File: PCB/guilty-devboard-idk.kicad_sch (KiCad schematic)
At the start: 66 parts, among them J1 USB_C_Receptacle_USB2.0_16P, Q1 SP2038CNQ, Q2 Q_PMOS, U1 nRF54LM20A-PAXX, U2 SGM40567-4.2XG/TR, U3 Xiao nRF52840 Connectors, U4 MIC2876-5.0YMT-TR, U5 FH9261-G3JH, U6 BD83070GWL-E2, Y1 32MHz, Y2 32.768kHz

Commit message: fully routed
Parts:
- removed C10: 4.7uF, Capacitor_SMD:C_0201_0603Metric, symbol KiCad:C_Small
- removed C20: 22uF, Capacitor_SMD:C_0201_0603Metric, symbol Device:C
- removed C22: 1uF, Capacitor_SMD:C_0201_0603Metric, symbol Device:C_Small
- removed D2, D3: D, Diode_SMD:D_SOD-882, symbol Device:D
- removed D4, D5: D, Diode_SMD:D_SOD-323, symbol Device:D
- removed JP2: Jumper_2_Bridged, Resistor_SMD:R_0201_0603Metric, symbol KiCad:Jumper_2_Bridged
- removed L2: 2.2uH, Inductor_SMD:L_0201_0603Metric, symbol Device:L_Small
- removed Q2: Q_PMOS, guilty-devboard-idk:Vishay_PowerPAK_SC70-6L_Single, symbol Device:Q_PMOS
- removed R13, R18: 1M, Resistor_SMD:R_0201_0603Metric, symbol Device:R_Small
- removed U1: nRF54LM20A-PAXX, PCM_nordic-lib-kicad-nrf54l:Nordic_FCCSP-98_3.67x3.85mm_Layout10x10_P0.35mm_Offcenter, symbol PCM_nordic-lib-kicad-nrf54l:nRF54LM20A-PAXX
- removed U3: Xiao nRF52840 Connectors, guilty-devboard-idk:Guilty Devboard Xrd pads, symbol guilty-devboard:Guilty Devboard Xrd Connectors (dev)
- removed U4: MIC2876-5.0YMT-TR, easyeda2kicad:UDFN-8_L2.0-W2.0-P0.50-BL-EP, symbol easyeda2kicad:MIC2876-5.0YMT-TR
- added JP1: Jumper_2_Open, Resistor_SMD:R_0603_1608Metric, symbol KiCad:Jumper_2_Open
- added U1: nRF54LM20A-QGAA, PCM_nordic-lib-kicad-nrf54l:QFN-52-1EP_6x6mm_P0.4mm_EP4.7x4.7mm_ThermalVias, symbol PCM_nordic-lib-kicad-nrf54l:nRF54LM20A-QGAA
- added U3: Xiao nRF52840 Connectors, guilty-devboard-idk:Xiao nRF52840 Plus pads, symbol guilty-devboard:Xiao nRF52840 Plus Connectors (dev)
- C16, C19: footprint Capacitor_SMD:C_0201_0603Metric -> Capacitor_SMD:C_0402_1005Metric
- L6: footprint Inductor_SMD:L_0201_0603Metric -> Inductor_SMD:L_0603_1608Metric
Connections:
- net +3V3: now also U1.42 (VDD), U1.51 (VDD), U1.6 (VDD), U3.10 (3V3)
- net +BATT: now also U3.24 (BAT+)
- net -BATT: now also U3.25 (BAT-)
- net ANT: now also U1.34 (ANT)
- net BATT_LEVEL: now also U1.10 (P1.00)
- net CHARGE_STATUS: now also U1.30 (P0.09)
- net FAST_CHARGE_1: now also U1.28 (P0.07)
- net FAST_CHARGE_2: now also U1.29 (P0.08)
- net GND: now also AE1.2 (PCB_Trace), JP1.2 (B), U1.35 (VSS), U1.45 (VSS), U1.53 (VSS), U3.29 (GND), U3.9 (GND)
- net P0.03_GRTC.PWM: now also U1.25 (P0.03), U3.21 (D19_MOSI1)
- net P0.04_GRTC.CLKOUT32K: now also U1.26 (P0.04), U3.23 (D17_SCK1)
- net P1.01_NFC1: now also U1.11 (P1.01), U3.18 (D14_NFC1)
- net P1.02_NFC2: now also U1.12 (P1.02), U3.19 (D15_NFC2)
- net P1.03_A/D0: now also U1.13 (P1.03), U3.1 (A/D0)
- net P1.04_A/D1: now also U1.14 (P1.04), U3.2 (A/D1)
- net P1.05_A/D2: now also U1.15 (P1.05), U3.3 (A/D2)
- net P1.06_A/D3: now also U1.16 (P1.06), U3.4 (A/D3)
- net P1.07_GRTC.CLKOUTFAST: now also U1.22 (P1.07), U3.22 (D18_MISO1)
- net P1.29_D16_A6: now also U1.7 (P1.29), U3.20 (D16_A6)
- net P1.30_A/D4_I2C_SDA: now also U1.8 (P1.30), U3.5 (A/D4_SDA)
- net P1.31_A/D5_I2C_SCL: now also U1.9 (P1.31), U3.6 (A/D5_SCL)
- net RESET: now also JP1.1 (A), U1.33 (~{RESET}), U3.28 (RST)
- net SWDCLK: now also U1.31 (SWDCLK), U3.27 (CLK)
- net SWDIO: now also U1.32 (SWDIO), U3.26 (DIO)
- net VBUS: now also U3.8 (5V)
- net at Y1.1: now also U1.37 (XC1)
- net at L6.1: now also U1.43 (DCC)
- net at C4.1, FB1.1, L6.2: now also U1.44 (DECD)
- net at C5.1, C6.1, C7.1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: now also U1.46 (DECA)
- net at Y1.3: now also U1.38 (XC2)
- net at C5.2, L7.1: now also U1.36 (DECRF)
- net at Y2.1: now also U1.48 (P1.20)
- net at Y2.3: now also U1.49 (P1.21)
- net at R17.2: now also U1.21 (TXRTUNE)
- net MCU_USB_D-: now reaches R5.2
- net MCU_USB_D-: now also U1.20 (D-)
- net MCU_USB_D+: now reaches R4.2
- net MCU_USB_D+: now also U1.19 (D+)
- net at C13.2: now also U1.18 (DECUSB)
- net at C11.1, R16.2: now also U1.17 (VBUS)
- new net P1.08_D12: U1.23 (P1.08), U3.16 (D12)
- new net P1.09_D6: U1.24 (P1.09), U3.7 (D6_TX)
- new net P1.15_D13: U1.39 (P1.15), U3.17 (D13)
- new net P2.00_SPIM.DCX_UARTE00.RXD: U1.52 (P2.00), U3.14 (D7_RX)
- new net P2.01_SPIM.SCK: U1.1 (P2.01), U3.13 (D8_SCK)
- new net P2.02_SPIM.MOSI/SDO_UARTE00.TXD: U1.2 (P2.02), U3.11 (D10_MOSI)
- new net P2.04_SPIM.MISO/SDI_UARTE00.CTS: U1.4 (P2.04), U3.12 (D9_MISO)
- new net P2.05_SPIM.CSN_UARTE00.RTS: U1.5 (P2.05), U3.15 (D11)
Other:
- note added: "TODO: - pcb it - double check decoupling routing - make sure to place crystals and antenna filter as close as possible to MCU - crystals can be far but that requires adjusting load capacitance and calculating trace capacitance is a huge pain - do fancy antennas stuff ofc (impedance match everything to 50 ohms) - add basic GPIO - put 5V input cap as close as possible - QSPI - match traces, do not 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"
- note removed: "5V power circuitry"
- note removed: "AGND would be AGND (connected to GND at *one* point) but this is the only thing using AGND so just connecting it to GND directly"
- note removed: "TODO: - add the rest of the gpio - does the other end of the antenna need GND? idk - pcb it - double check decoupling routing - make sure to place crystals and antenna filter as close as possible to MCU - crystals can be far but that requires adjusting load capacitance and calculating trace capacitance is a huge pain - do fancy antennas stuff ofc (impedance match everything to 50 ohms) - add basi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"
- note removed: "TODO: when wiring rear GPIO, wire INTa/b and addresses (if possible) to GPIO too!!!"
- note removed: "capacitors should be as close as possible"
- note removed: "connect /PG to AGND if unused"
- note removed: "could use EN pin to enable/disable, but only accepts up to VIN, and if on USB, then VBUS is applied, and VBUS > VIN so to make it work would require running USB through it, which would be more complex and more inefficient to make it work at all would take more components than it saves"
- note removed: "note 4.8A switching current != 4.8A output current absolute theoretical max ~2.5A output current this diode is only rated for 2A and i only guarantee 1A based off datahseet"
- note removed: "recommended 4.7+ uF ^^^ capacitor here as close as possible to inductor and connected to PGND, but not required"
- note removed: "so you can design a PCB using this such that you can swap it out for a standard xiao and lose minimal functionality"
- moved on the sheet: C5, C6, C7, L7, R4, R5

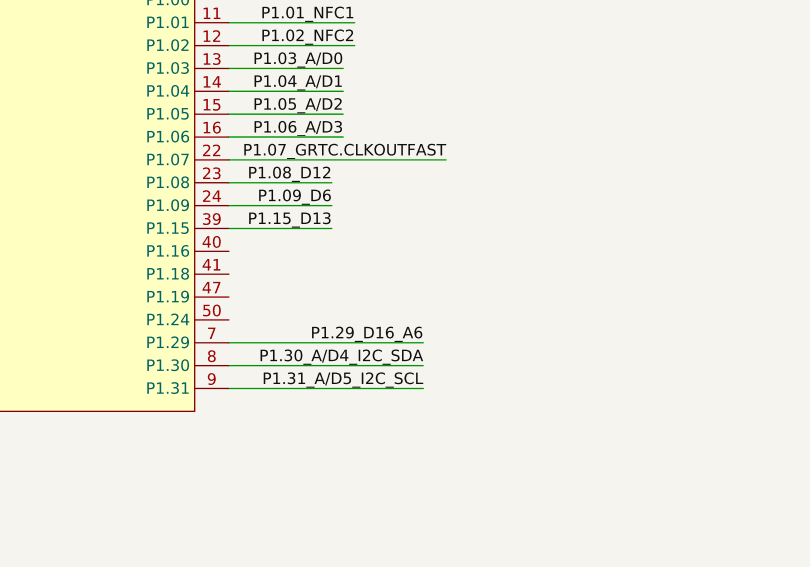
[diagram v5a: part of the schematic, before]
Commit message: update routing to make antenna better
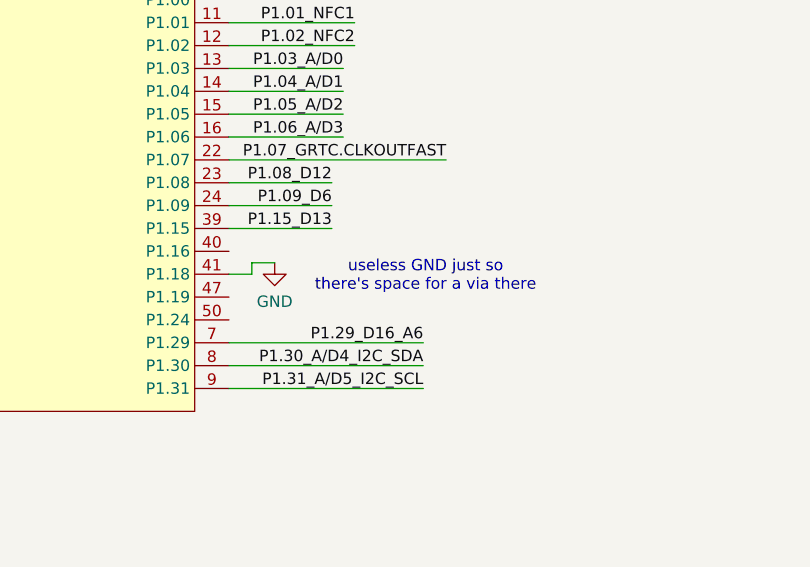
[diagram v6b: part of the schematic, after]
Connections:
- net GND: now also U1.41 (P1.18)
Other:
- note added: "useless GND just so there's space for a via there"
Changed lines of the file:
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@@
 		)
 	)
+	(text "useless GND just so \nthere's space for a via there"
+		(exclude_from_sim no)
+		(at 350.774 301.244 0)
+		(effects
+			(font
+				(size 1.27 1.27)
+			)
+		)
+	)
 	(junction
 		(at 236.22 55.88)
@@
 	(wire
 		(pts
+			(xy 331.47 299.72) (xy 334.01 299.72)
+		)
+		(stroke
+			(width 0)
+			(type default)
+		)
+	)
+	(wire
+		(pts
 			(xy 273.05 59.69) (xy 264.16 59.69)
 		)
@@
 	(wire
 		(pts
+			(xy 331.47 300.99) (xy 331.47 299.72)
+		)
+		(stroke
+			(width 0)
+			(type default)
+		)
+	)
+	(wire
+		(pts
 			(xy 76.2 49.53) (xy 92.71 49.53)
 		)
@@
 	(wire
 		(pts
+			(xy 328.93 300.99) (xy 331.47 300.99)
+		)
+		(stroke
+			(width 0)
+			(type default)
+		)
+	)
+	(wire
+		(pts
 			(xy 36.83 22.86) (xy 48.26 22.86)
 		)
@@
 					(unit 1)
 				)
+			)
+		)
+	)
+	(symbol
+		(lib_id "KiCad:GND")
+		(at 334.01 299.72 0)
+		(unit 1)
+		(body_style 1)
+		(exclude_from_sim no)
+		(in_bom yes)
+		(on_board yes)
+		(in_pos_files yes)
+		(dnp no)
+		(property "Reference" "#PWR014"
+			(at 334.01 306.07 0)
+			(hide yes)
+			(show_name no)
+			(do_not_autoplace no)
+			(effects
+				(font
+					(size 1.27 1.27)
+				)
+			)
+		)
+		(property "Value" "GND"
+			(at 334.01 304.038 0)
+			(show_name no)
+			(do_not_autoplace no)
+			(effects
+				(font
+					(size 1.27 1.27)
+				)
+			)
+		)
+		(property "Footprint" ""
+			(at 334.01 299.72 0)
+			(hide yes)
+			(show_name no)
+			(do_not_autoplace no)
+			(effects
+				(font
+					(size 1.27 1.27)
+				)
+			)
+		)
+		(property "Datasheet" ""
+			(at 334.01 299.72 0)
+			(hide yes)
+			(show_name no)
+			(do_not_autoplace no)
+			(effects
+				(font
+					(size 1.27 1.27)
+				)
+			)
+		)
+		(property "Description" "Power symbol creates a global label with name \"GND\" , ground"
+			(at 334.01 299.72 0)
+			(hide yes)
+			(show_name no)
+			(do_not_autoplace no)
+			(effects
+				(font
+					(size 1.27 1.27)
+				)
+			)
+		)
+		(pin "1"
+		)
+		(instances
+			(project "guilty-devboard-idk"
+				(path "/f655de09-440b-4c8a-8451-7845142cd85d"
+					(reference "#PWR014")
+					(unit 1)
+				)

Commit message: misc notes and whatnot on schematic, got rid of unnecessary via/GNDed pin
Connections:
- net GND: no longer U1.41 (P1.18)
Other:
- note added: "- pcb it √ - double check decoupling routing √ - make sure to place crystals and antenna filter as close as possible to MCU √ - crystals can be far but that requires adjusting load capacitance and calculating trace capacitance is a huge pain - do fancy antennas stuff ofc (impedance match everything to 50 ohms) √ - do via fencing and isolate everything as well as possible √ - add basic GPIO √"
- note added: "jumper is used instead of a button because i couldn't find a switch that small"
- note added: "most likely only one of this board will ever exist, maybe 5, all manually produced; the choice to add or not add the voltage divider can be made later (this matters because of power draw and, externally, using up GPIO)"
- note added: "this specific variant is the best i could find but if necessary, could probably use any other FH9261 variant just check the datasheets"
- note removed: "Notes potential power savings: - make voltage divider more efficient? - remove voltage divider entirely? - boards using original xiao will need a separate one anyways, and this allows for easier testing of different resistor values to see what works"
- note removed: "TODO: - pcb it - double check decoupling routing - make sure to place crystals and antenna filter as close as possible to MCU - crystals can be far but that requires adjusting load capacitance and calculating trace capacitance is a huge pain - do fancy antennas stuff ofc (impedance match everything to 50 ohms) - add basic GPIO - put 5V input cap as close as possible - QSPI - match traces, do not 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"
- note removed: "TODO: check power savings"
- note removed: "useless GND just so there's space for a via there"
- moved on the sheet: C12, Q1A, Q1B, R6, R7, R8, R9, U5

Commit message: add 5mm edges for pcba
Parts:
- R17: Tolerance (none) -> ±1%
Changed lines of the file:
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@@
 	)
 	(junction
-		(at 313.69 44.45)
-		(diameter 0)
-		(color 0 0 0 0)
-	)
-	(junction
 		(at 449.58 176.53)
 		(diameter 0)
@@
 	)
 	(junction
-		(at 313.69 34.29)
-		(diameter 0)
-		(color 0 0 0 0)
-	)
-	(junction
 		(at 55.88 233.68)
 		(diameter 0)
@@
 	(wire
 		(pts
-			(xy 316.23 43.18) (xy 313.69 44.45)
-		)
-		(stroke
-			(width 0)
-			(type default)
-		)
-	)
-	(wire
-		(pts
 			(xy 83.82 87.63) (xy 76.2 87.63)
 		)
@@
 	(wire
 		(pts
-			(xy 316.23 33.02) (xy 313.69 34.29)
-		)
-		(stroke
-			(width 0)
-			(type default)
-		)
-	)
-	(wire
-		(pts
 			(xy 106.68 261.62) (xy 118.11 261.62)
 		)
@@
 				)
 			)
+		)
+		(property "Tolerance" "±1%"
+			(at 29.718 86.106 90)
+			(show_name no)
+			(do_not_autoplace no)
+			(effects
+				(font
+					(size 1 1)
+				)
+			)
